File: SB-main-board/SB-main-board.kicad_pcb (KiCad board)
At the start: 4 copper layers, 53 x 40 mm, 94 parts, among them J1 XT30PB_IN, J2 Download, J3 Excluder, J4 PT100, J5 Hotend, J6 FAN2, J7 LDC, J8 FS, J9 FAN, Q1 BUK9M4R3-40H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

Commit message: layout: swap the led and the resistor
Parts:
- moved D4 1.01 mm to (102.7, 83.8), turned to 0 degrees
- moved R18 1.01 mm to (102.7, 82.8), turned to 180 degrees
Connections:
- D4 pad 2: Net-(D4-A) -> +24V
- J5 pad 2: Net-(D4-K) -> Net-(J5-Pin_2)
- Q1 pad 5: Net-(D4-K) -> Net-(J5-Pin_2)
- R18 pad 1: Net-(D4-A) -> Net-(J5-Pin_2)
- R18 pad 2: +24V -> Net-(D4-K)
- TP2 pad 1: Net-(D4-K) -> Net-(J5-Pin_2)
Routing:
- net Net-(J5-Pin_2): track 0.00 -> 1.74 mm, vias 0 -> 11
- net Net-(D4-A): track 1.01 -> 0.00 mm
- net Net-(D4-K): track 1.74 -> 1.01 mm, vias 11 -> 0
- net GND: vias 152 -> 154
- added copper zone on B.Cu, net Net-(J5-Pin_2)
- added copper zone on F.Cu, net Net-(J5-Pin_2)
- added copper zone on In1.Cu, net Net-(J5-Pin_2)
- added copper zone on In2.Cu, net Net-(J5-Pin_2)
- removed copper zone on B.Cu, net Net-(D4-K)
- removed copper zone on F.Cu, net Net-(D4-K)
- removed copper zone on In1.Cu, net Net-(D4-K)
- removed copper zone on In2.Cu, net Net-(D4-K)

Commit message: layout: optime the routes for TMC2209
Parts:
- moved C23 2.06 mm to (109.0, 74.5)
- moved C24 2.06 mm to (111.8, 74.5)
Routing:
- net +24V: track 79.3 -> 75.2 mm
- net GND: track 10.7 -> 11.2 mm, vias 154 -> 156

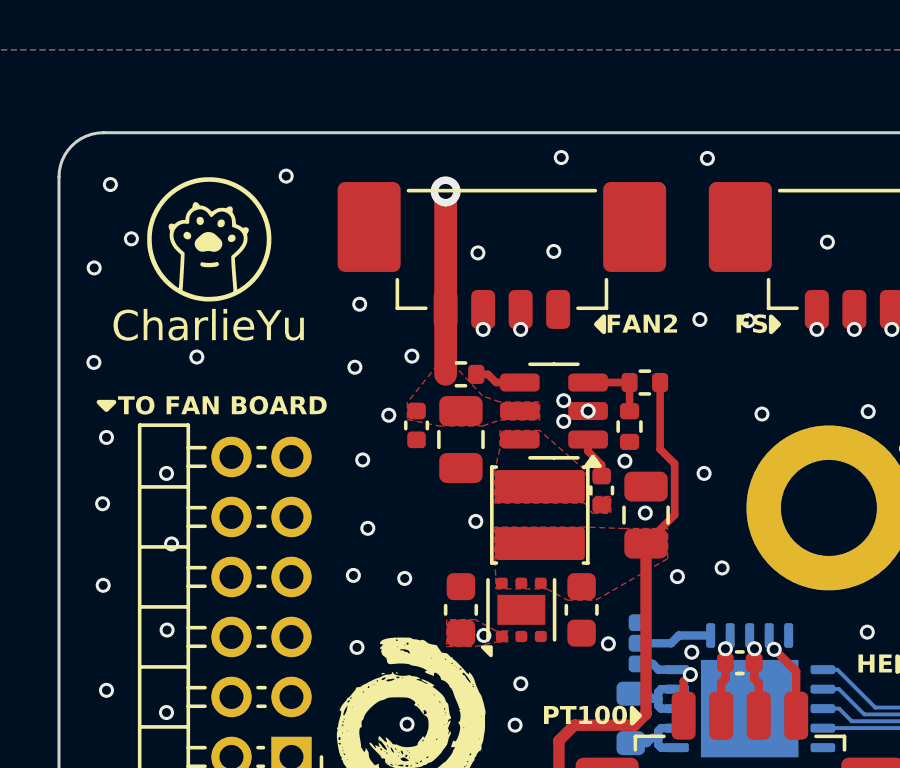
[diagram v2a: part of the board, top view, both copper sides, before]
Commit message: footprint: change input cap to 1206
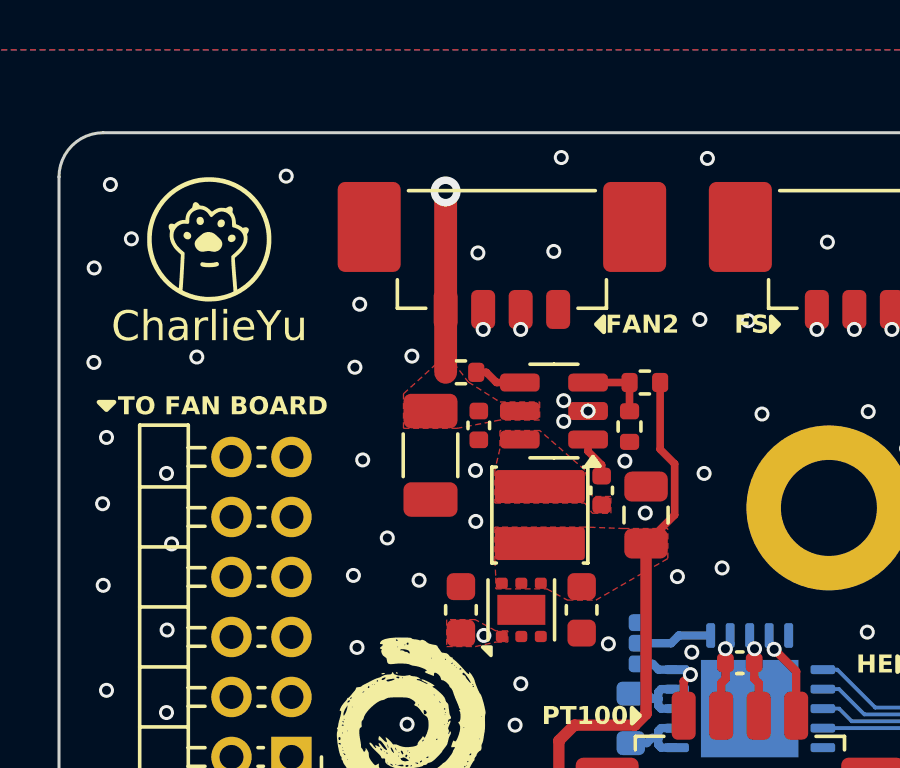
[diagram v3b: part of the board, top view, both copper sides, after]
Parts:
- C16: footprint Capacitor_SMD:C_0805_2012Metric -> Capacitor_SMD:C_1206_3216Metric
- moved C35 2.08 mm to (86.4, 77.4)
- moved C16 1.14 mm to (84.8, 78.4)
- moved R11 0.07 mm to (85.8, 75.6)

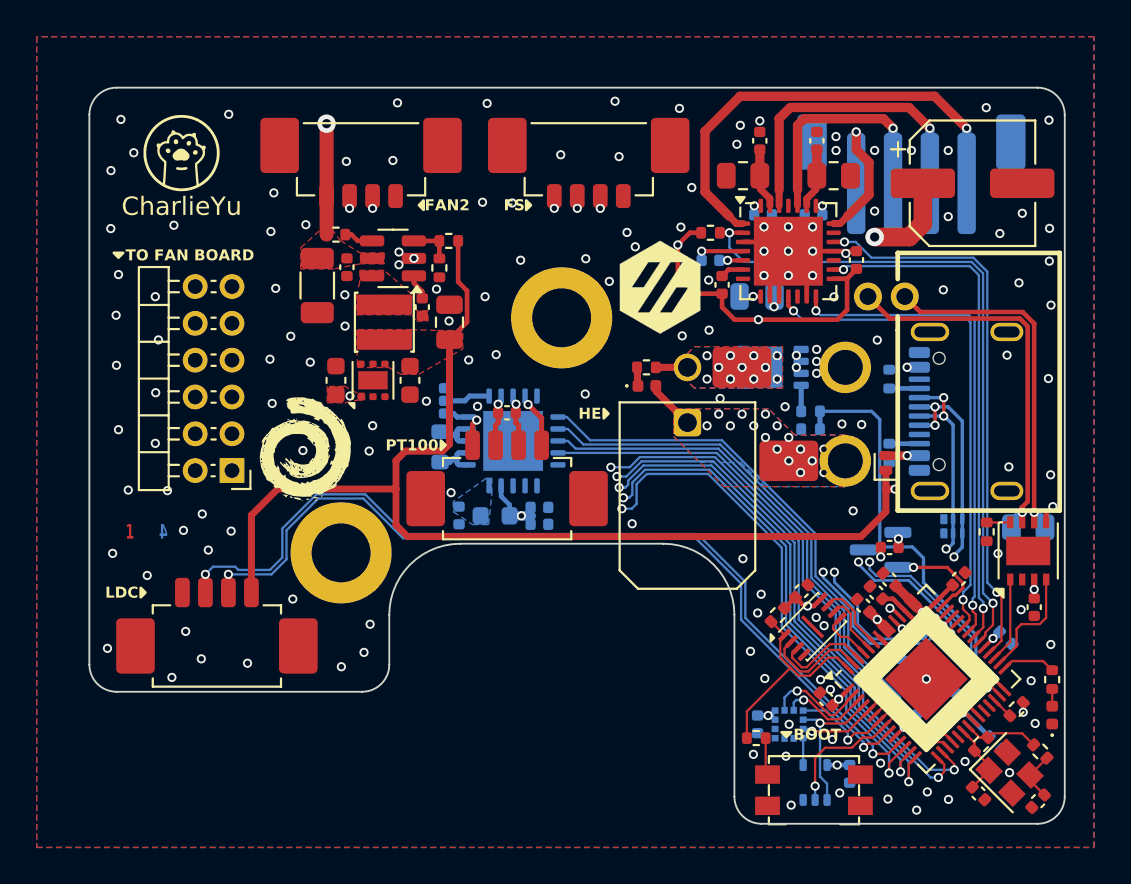
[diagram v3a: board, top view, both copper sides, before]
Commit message: layout: optmise layout silkscreen: change silkscreen
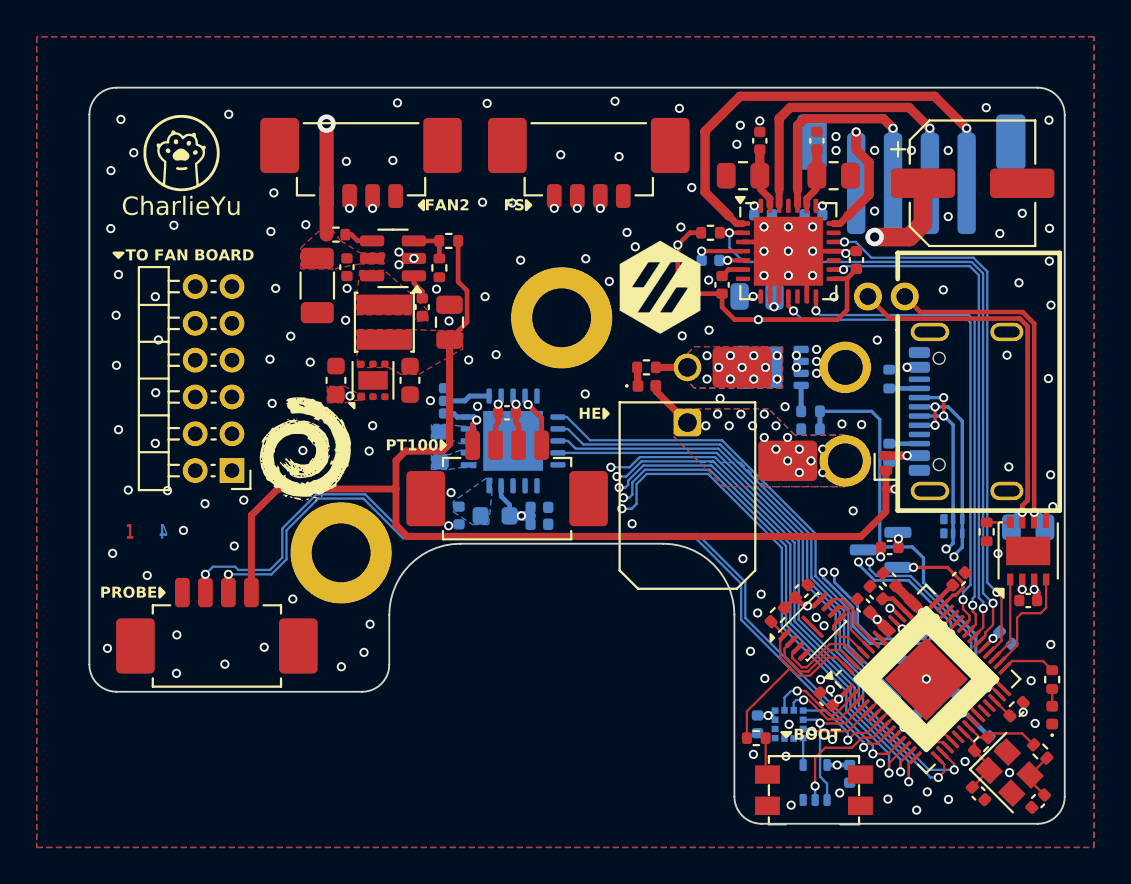
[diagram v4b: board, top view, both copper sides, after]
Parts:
- added G6: ESD-Logo_6.6x6mm_SilkScreen, Symbol:ESD-Logo_6.6x6mm_SilkScreen, B.Cu at (79.9, 92.4)
- moved C31 0.92 mm to (96.9, 91.3)
- moved C32 0.92 mm to (96.9, 90.4)
- moved C14 0.49 mm to (123.4, 95.5), turned to 180 degrees
- moved TP1 0.06 mm to (110.4, 87.9)
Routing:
- net Net-(U9-ISENSOR): track 2.75 -> 0.00 mm
- net Net-(U9-BIAS): track 2.75 -> 0.00 mm
- net GND: vias 156 -> 157
- added copper zone on B.Cu, net Net-(U9-BIAS)
- added copper zone on B.Cu, net Net-(U9-ISENSOR)
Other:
- board text added: "2W/4W"
- board text added: "3W"
- board text added: "PROBE"
- board text added: "不能捡"
- board text removed: "Close upper jumpper when using 2W/4W or Close the lower one"
- board text removed: "LDC"

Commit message: misc: fix typo
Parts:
- R16: value 220mR -> 200mR
